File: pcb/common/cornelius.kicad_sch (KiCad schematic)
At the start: 116 parts, among them J1 AVR-ISP-6, SW1 SW_Push, U1 ATmega32U4-M, U2 PRTR5V0U2X, Y1 16MHz

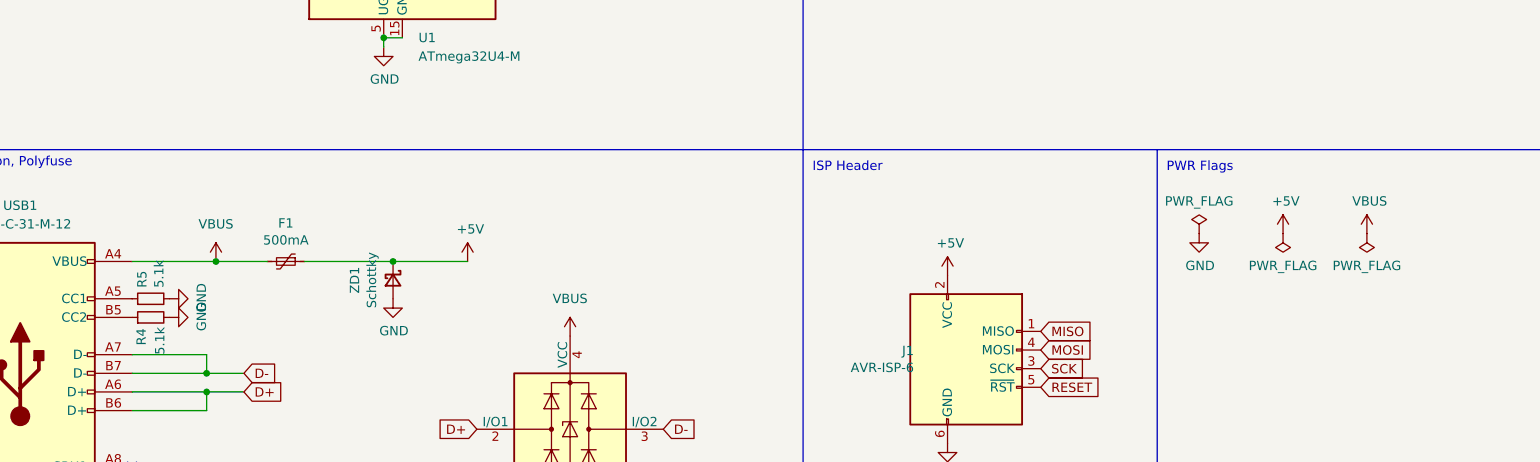
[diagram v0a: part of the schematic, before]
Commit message: Fix pass capacitor
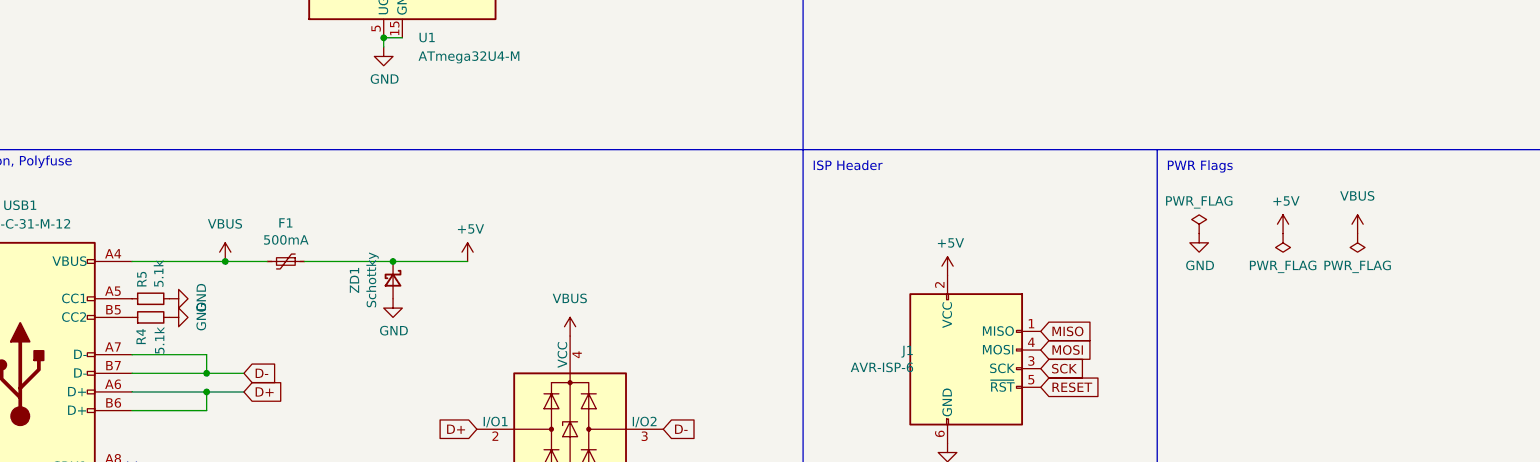
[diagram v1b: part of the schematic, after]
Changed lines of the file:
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@@
   (junction (at 320.04 92.71) (diameter 0) (color 0 0 0 0)
   )
-  (junction (at 63.5 148.59) (diameter 0) (color 0 0 0 0)
-  )
   (junction (at 274.32 59.69) (diameter 0) (color 0 0 0 0)
   )
@@
   (junction (at 299.72 54.61) (diameter 0) (color 0 0 0 0)
   )
+  (junction (at 64.77 148.59) (diameter 0) (color 0 0 0 0)
+  )
   (junction (at 223.52 87.63) (diameter 0) (color 0 0 0 0)
   )
@@
     (stroke (width 0) (type default))
   )
-  (wire (pts (xy 52.07 148.59) (xy 63.5 148.59))
-    (stroke (width 0) (type default))
-  )
   (wire (pts (xy 62.23 163.83) (xy 67.31 163.83))
     (stroke (width 0) (type default))
@@
     (stroke (width 0) (type default))
   )
-  (wire (pts (xy 63.5 148.59) (xy 70.485 148.59))
+  (wire (pts (xy 52.07 148.59) (xy 64.77 148.59))
     (stroke (width 0) (type default))
   )
@@
     (stroke (width 0) (type default))
   )
+  (wire (pts (xy 64.77 148.59) (xy 70.485 148.59))
+    (stroke (width 0) (type default))
+  )
   (wire (pts (xy 62.23 67.31) (xy 73.66 67.31))
     (stroke (width 0) (type default))
@@
     )
   )
+  (symbol (lib_id "power:PWR_FLAG") (at 219.075 144.78 180) (unit 1)
+    (in_bom yes) (on_board yes) (dnp no)
+    (property "Reference" "#FLG02" (at 219.075 146.685 0)
+      (effects (font (size 1.27 1.27)) hide)
+    )
+    (property "Value" "PWR_FLAG" (at 219.075 149.1742 0)
+      (effects (font (size 1.27 1.27)))
+    )
+    (property "Footprint" "" (at 219.075 144.78 0)
+      (effects (font (size 1.27 1.27)) hide)
+    )
+    (property "Datasheet" "~" (at 219.075 144.78 0)
+      (effects (font (size 1.27 1.27)) hide)
+    )
+    (pin "1")
+    (instances
+      (project "cornelius"
+        (path "/13e40788-c997-49b6-a295-2e0f727db597/6b5635e7-5fcf-47f3-9ba2-4889ebab0035"
+          (reference "#FLG02") (unit 1)
+        )
+      )
+      (project "cornelius"
+        (path "/195be91b-8e8a-44dc-96de-003bfb3dcf19/3f59913e-69da-4ba6-9eb9-394ebb2edc66"
+          (reference "#FLG03") (unit 1)
+        )
+      )
+      (project "cornelius"
+        (path "/2ec4f4fa-8c08-458a-8dcd-8bbe89e58c6a"
+          (reference "#FLG02") (unit 1)
+        )
+      )
+    )
+  )
   (symbol (lib_id "Switch:SW_Push") (at 340.36 104.14 180) (unit 1)
     (in_bom yes) (on_board yes) (dnp no) (fields_autoplaced)
@@
     )
   )
-  (symbol (lib_id "power:VBUS") (at 220.345 144.78 0) (unit 1)
-    (in_bom yes) (on_board yes) (dnp no)
-    (property "Reference" "#PWR022" (at 220.345 148.59 0)
-      (effects (font (size 1.27 1.27)) hide)
-    )
-    (property "Value" "VBUS" (at 220.726 140.3858 0)
-      (effects (font (size 1.27 1.27)))
-    )
-    (property "Footprint" "" (at 220.345 144.78 0)
-      (effects (font (size 1.27 1.27)) hide)
-    )
-    (property "Datasheet" "" (at 220.345 144.78 0)
-      (effects (font (size 1.27 1.27)) hide)
-    )
-    (pin "1")
-    (instances
-      (project "cornelius"
-        (path "/13e40788-c997-49b6-a295-2e0f727db597/6b5635e7-5fcf-47f3-9ba2-4889ebab0035"
-          (reference "#PWR022") (unit 1)
-        )
-      )
-      (project "cornelius"
-        (path "/195be91b-8e8a-44dc-96de-003bfb3dcf19/3f59913e-69da-4ba6-9eb9-394ebb2edc66"
-          (reference "#PWR022") (unit 1)
-        )
-      )
-      (project "cornelius"
-        (path "/2ec4f4fa-8c08-458a-8dcd-8bbe89e58c6a"
-          (reference "#PWR022") (unit 1)
-        )
-      )
-    )
-  )
   (symbol (lib_id "Device:D_Small") (at 243.84 90.17 90) (unit 1)
     (in_bom yes) (on_board yes) (dnp no)
@@
     )
   )
-  (symbol (lib_id "power:VBUS") (at 63.5 148.59 0) (unit 1)
-    (in_bom yes) (on_board yes) (dnp no) (fields_autoplaced)
-    (property "Reference" "#PWR019" (at 63.5 152.4 0)
-      (effects (font (size 1.27 1.27)) hide)
-    )
-    (property "Value" "VBUS" (at 63.5 143.51 0)
-      (effects (font (size 1.27 1.27)))
-    )
-    (property "Footprint" "" (at 63.5 148.59 0)
-      (effects (font (size 1.27 1.27)) hide)
-    )
-    (property "Datasheet" "" (at 63.5 148.59 0)
-      (effects (font (size 1.27 1.27)) hide)
-    )
-    (pin "1")
-    (instances
-      (project "cornelius"
-        (path "/13e40788-c997-49b6-a295-2e0f727db597/6b5635e7-5fcf-47f3-9ba2-4889ebab0035"
-          (reference "#PWR019") (unit 1)
-        )
-      )
-      (project "cornelius"
-        (path "/195be91b-8e8a-44dc-96de-003bfb3dcf19/3f59913e-69da-4ba6-9eb9-394ebb2edc66"
-          (reference "#PWR019") (unit 1)
-        )
-      )
-      (project "cornelius"
-        (path "/2ec4f4fa-8c08-458a-8dcd-8bbe89e58c6a"
-          (reference "#PWR05") (unit 1)
-        )
-      )
-    )
-  )
   (symbol (lib_id "Device:D_Small") (at 213.36 73.66 90) (unit 1)
     (in_bom yes) (on_board yes) (dnp no)
@@
     )
   )
-  (symbol (lib_id "power:PWR_FLAG") (at 220.345 144.78 180) (unit 1)
-    (in_bom yes) (on_board yes) (dnp no)
-    (property "Reference" "#FLG03" (at 220.345 146.685 0)
-      (effects (font (size 1.27 1.27)) hide)
-    )
-    (property "Value" "PWR_FLAG" (at 220.345 149.1742 0)
-      (effects (font (size 1.27 1.27)))
-    )
-    (property "Footprint" "" (at 220.345 144.78 0)
-      (effects (font (size 1.27 1.27)) hide)
-    )
-    (property "Datasheet" "~" (at 220.345 144.78 0)
-      (effects (font (size 1.27 1.27)) hide)
-    )
-    (pin "1")
-    (instances
-      (project "cornelius"
-        (path "/13e40788-c997-49b6-a295-2e0f727db597/6b5635e7-5fcf-47f3-9ba2-4889ebab0035"
-          (reference "#FLG03") (unit 1)
-        )
-      )
-      (project "cornelius"
-        (path "/195be91b-8e8a-44dc-96de-003bfb3dcf19/3f59913e-69da-4ba6-9eb9-394ebb2edc66"
-          (reference "#FLG03") (unit 1)
-        )
-      )
-      (project "cornelius"
-        (path "/2ec4f4fa-8c08-458a-8dcd-8bbe89e58c6a"
-          (reference "#FLG03") (unit 1)
-        )
-      )
-    )
-  )
   (symbol (lib_id "Device:D_Small") (at 243.84 106.68 90) (unit 1)
     (in_bom yes) (on_board yes) (dnp no)
@@
     )
   )
+  (symbol (lib_id "power:VBUS") (at 64.77 148.59 0) (unit 1)
+    (in_bom yes) (on_board yes) (dnp no) (fields_autoplaced)
+    (property "Reference" "#PWR013" (at 64.77 152.4 0)
+      (effects (font (size 1.27 1.27)) hide)
+    )
+    (property "Value" "VBUS" (at 64.77 143.51 0)
+      (effects (font (size 1.27 1.27)))
+    )
+    (property "Footprint" "" (at 64.77 148.59 0)
+      (effects (font (size 1.27 1.27)) hide)
+    )
+    (property "Datasheet" "" (at 64.77 148.59 0)
+      (effects (font (size 1.27 1.27)) hide)
+    )
+    (pin "1")
+    (instances
+      (project "cornelius"
+        (path "/195be91b-8e8a-44dc-96de-003bfb3dcf19/3f59913e-69da-4ba6-9eb9-394ebb2edc66"
+          (reference "#PWR013") (unit 1)
+        )
+      )
+    )
+  )
   (symbol (lib_id "Device:D_Small") (at 304.8 90.17 90) (unit 1)
     (in_bom yes) (on_board yes) (dnp no)
@@
     )
   )
+  (symbol (lib_id "power:VBUS") (at 219.075 144.78 0) (unit 1)
+    (in_bom yes) (on_board yes) (dnp no) (fields_autoplaced)
+    (property "Reference" "#PWR05" (at 219.075 148.59 0)
+      (effects (font (size 1.27 1.27)) hide)
+    )
+    (property "Value" "VBUS" (at 219.075 139.7 0)
+      (effects (font (size 1.27 1.27)))
+    )
+    (property "Footprint" "" (at 219.075 144.78 0)
+      (effects (font (size 1.27 1.27)) hide)
+    )
+    (property "Datasheet" "" (at 219.075 144.78 0)
+      (effects (font (size 1.27 1.27)) hide)
+    )
+    (pin "1")
+    (instances
+      (project "cornelius"
+        (path "/195be91b-8e8a-44dc-96de-003bfb3dcf19/3f59913e-69da-4ba6-9eb9-394ebb2edc66"
+          (reference "#PWR05") (unit 1)
+        )
+      )
+    )
+  )
   (symbol (lib_id "Switch:SW_Push") (at 233.68 54.61 180) (unit 1)
     (in_bom yes) (on_board yes) (dnp no) (fields_autoplaced)
@@
     )
   )
+  (symbol (lib_id "power:VBUS") (at 111.76 158.75 0) (unit 1)
+    (in_bom yes) (on_board yes) (dnp no) (fields_autoplaced)
+    (property "Reference" "#PWR01" (at 111.76 162.56 0)
+      (effects (font (size 1.27 1.27)) hide)
+    )
+    (property "Value" "VBUS" (at 111.76 153.67 0)
+      (effects (font (size 1.27 1.27)))
+    )
+    (property "Footprint" "" (at 111.76 158.75 0)
+      (effects (font (size 1.27 1.27)) hide)
+    )
+    (property "Datasheet" "" (at 111.76 158.75 0)
+      (effects (font (size 1.27 1.27)) hide)
+    )
+    (pin "1")
+    (instances
+      (project "cornelius"
+        (path "/195be91b-8e8a-44dc-96de-003bfb3dcf19/3f59913e-69da-4ba6-9eb9-394ebb2edc66"
+          (reference "#PWR01") (unit 1)
+        )
+      )
+    )
+  )
   (symbol (lib_id "Switch:SW_Push") (at 218.44 71.12 180) (unit 1)
     (in_bom yes) (on_board yes) (dnp no) (fields_autoplaced)
@@
       (project "cornelius"
         (path "/195be91b-8e8a-44dc-96de-003bfb3dcf19/3f59913e-69da-4ba6-9eb9-394ebb2edc66"
-          (reference "#PWR02") (unit 1)
+          (reference "#PWR0102") (unit 1)
         )
       )
@@
         )
       )
-    )
-  )
-  (symbol (lib_id "power:VBUS") (at 111.76 158.75 0) (unit 1)
-    (in_bom yes) (on_board yes) (dnp no) (fields_autoplaced)
-    (property "Reference" "#PWR019" (at 111.76 162.56 0)
-      (effects (font (size 1.27 1.27)) hide)
-    )
-    (property "Value" "VBUS" (at 111.76 153.67 0)
-      (effects (font (size 1.27 1.27)))
-    )
-    (property "Footprint" "" (at 111.76 158.75 0)
-      (effects (font (size 1.27 1.27)) hide)
-    )
-    (property "Datasheet" "" (at 111.76 158.75 0)
-      (effects (font (size 1.27 1.27)) hide)
-    )
-    (pin "1")
-    (instances
-      (project "cornelius"
-        (path "/13e40788-c997-49b6-a295-2e0f727db597/6b5635e7-5fcf-47f3-9ba2-4889ebab0035"
-          (reference "#PWR019") (unit 1)
-        )
-      )
-      (project "cornelius"
-        (path "/195be91b-8e8a-44dc-96de-003bfb3dcf19/3f59913e-69da-4ba6-9eb9-394ebb2edc66"
-          (reference "#PWR019") (unit 1)
-        )
-      )
-      (project "cornelius"
-        (path "/2ec4f4fa-8c08-458a-8dcd-8bbe89e58c6a"
-          (reference "#PWR013") (unit 1)
-        )
-      )
